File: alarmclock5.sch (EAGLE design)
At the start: 44 parts, among them Q1 FDN360P, T1 2N2222, X1 MKDSN1,5/2-5,08, X2 MKDSN1,5/2-5,08, X3 MKDSN1,5/2-5,08, X4 MKDSN1,5/2-5,08

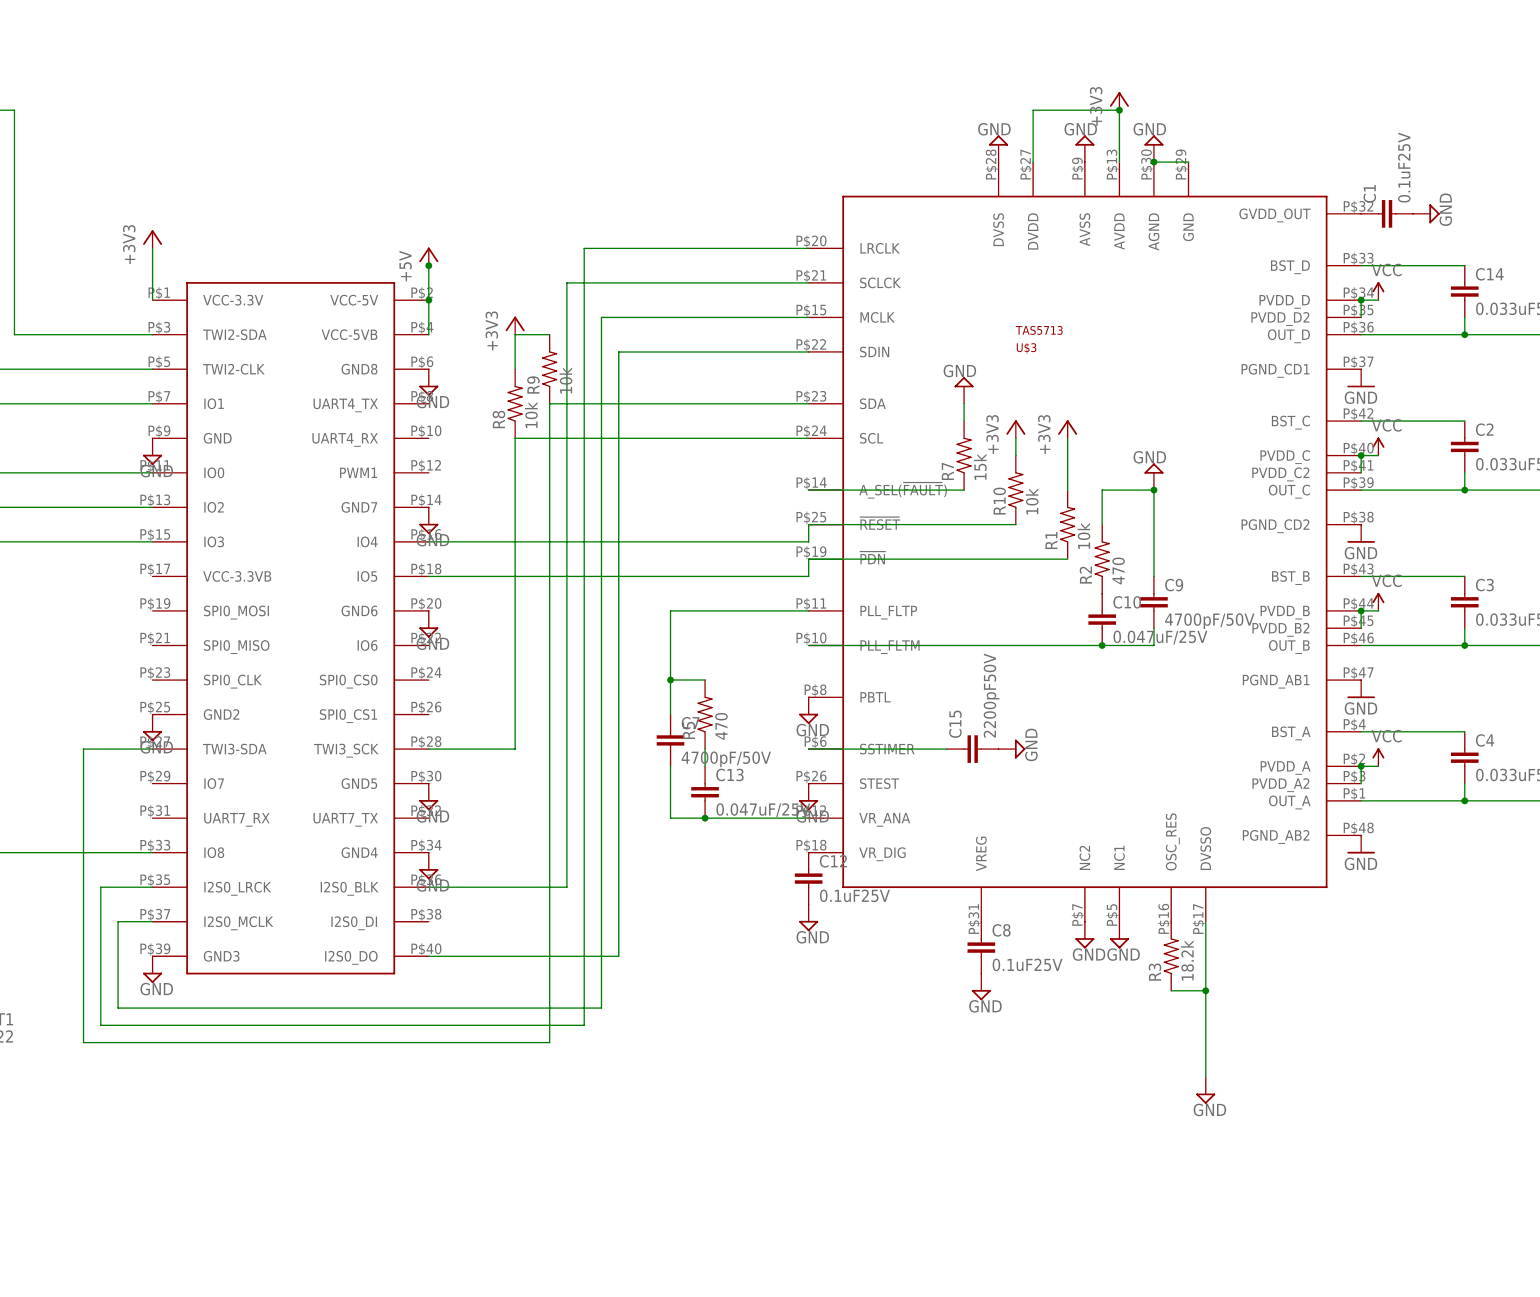
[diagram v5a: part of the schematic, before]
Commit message: new decoupling capa
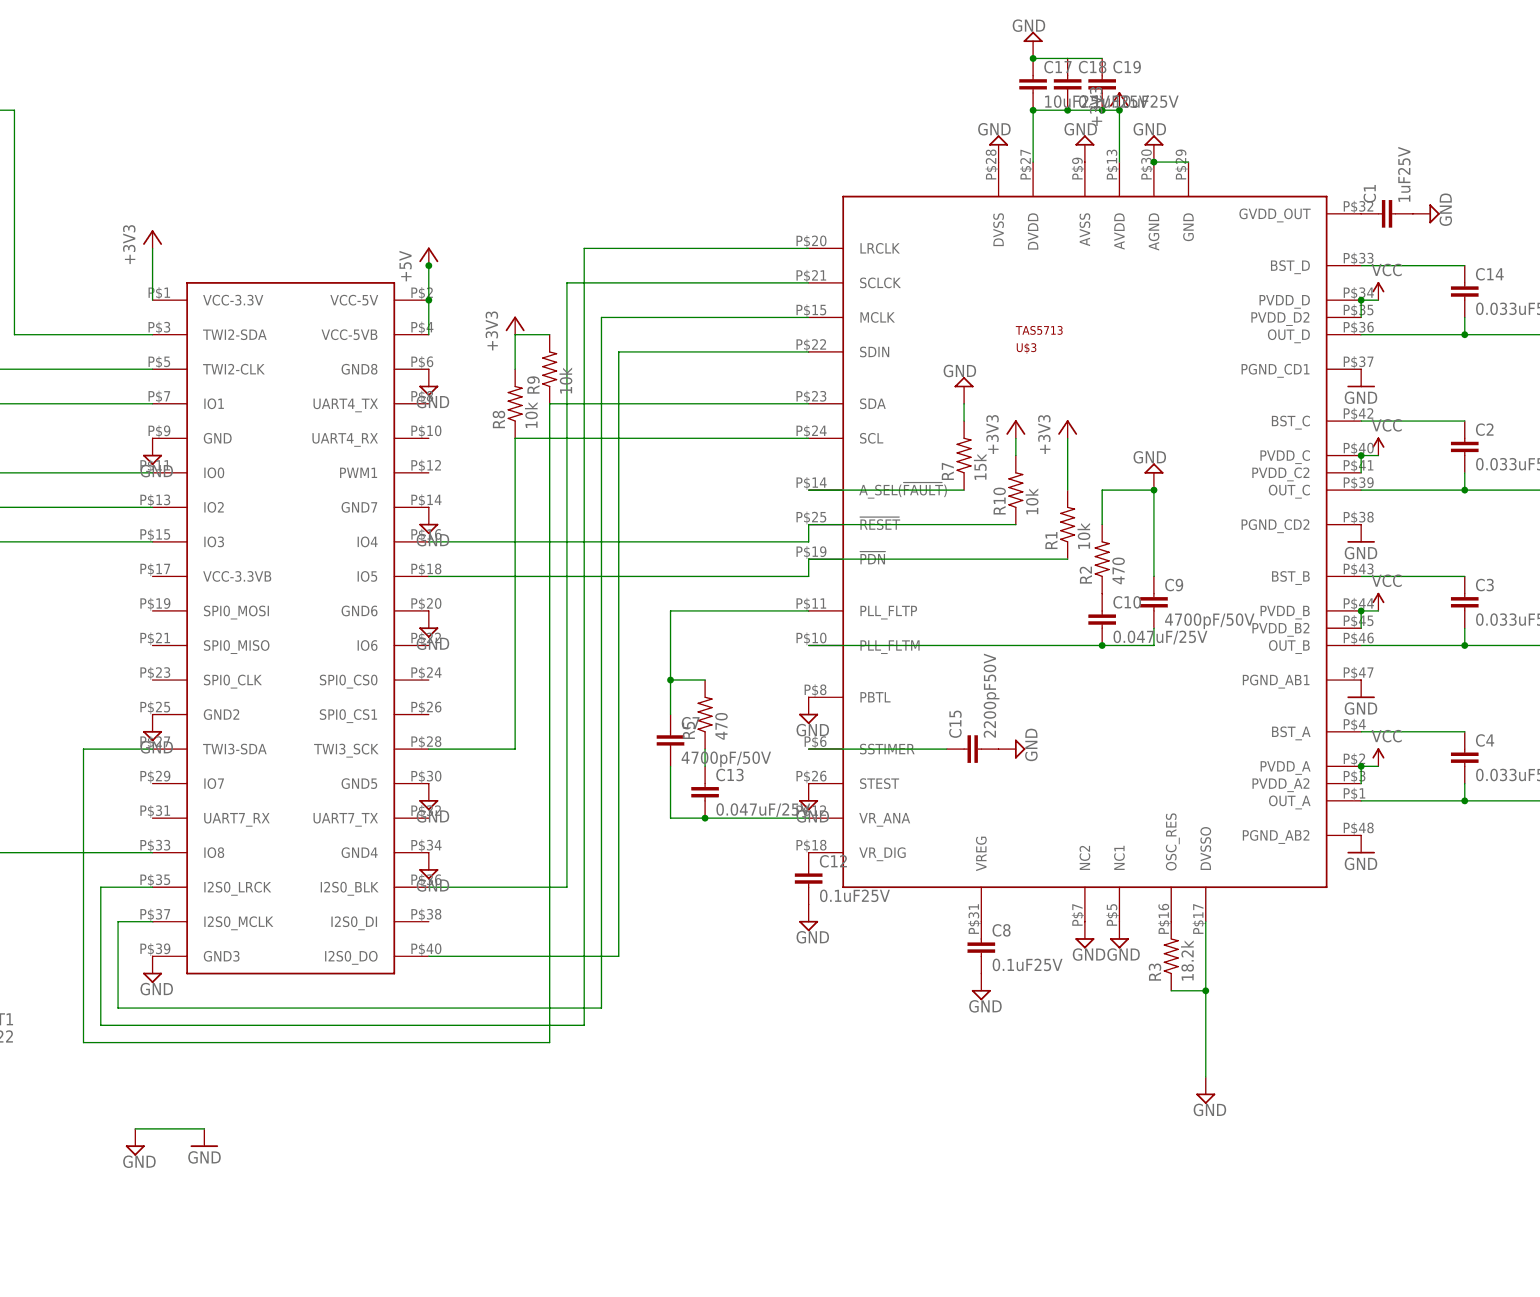
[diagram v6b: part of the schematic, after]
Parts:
- added C17, C19: 10uF25V, SparkFun-Capacitors:CAP0603-CAP
- added C18: 0.1uF25V, SparkFun-Capacitors:CAP0603-CAP
- C1: value 0.1uF25V -> 1uF25V
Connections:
- net +3V3: now also C17.2, C18.2, C19.2
- net GND: now also C17.1, C18.1, C19.1
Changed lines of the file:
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@@
 <part name="+3V8" library="supply1" deviceset="+3V3" device=""/>
 <part name="R10" library="SparkFun-Passives" deviceset="RESISTOR" device="0603-RES" value="10k"/>
-<part name="C1" library="SparkFun-Capacitors" deviceset="CAP" device="0603-CAP" value="0.1uF25V"/>
+<part name="C1" library="SparkFun-Capacitors" deviceset="CAP" device="0603-CAP" value="1uF25V"/>
 <part name="SUPPLY18" library="supply2" deviceset="GND" device=""/>
 <part name="C15" library="SparkFun-Capacitors" deviceset="CAP" device="0603-CAP" value="2200pF50V"/>
@@
 <part name="C16" library="SparkFun-Passives" deviceset="CAP_POL" device="PTH2" value="680uF/25V"/>
 <part name="R12" library="SparkFun-Passives" deviceset="RESISTOR" device="0603-RES" value="10k"/>
+<part name="SUPPLY1" library="supply2" deviceset="GND" device=""/>
+<part name="GND6" library="SparkFun-Aesthetics" deviceset="GND" device=""/>
+<part name="C17" library="SparkFun-Capacitors" deviceset="CAP" device="0603-CAP" value="10uF25V"/>
+<part name="SUPPLY32" library="supply2" deviceset="GND" device=""/>
+<part name="C18" library="SparkFun-Capacitors" deviceset="CAP" device="0603-CAP" value="0.1uF25V"/>
+<part name="C19" library="SparkFun-Capacitors" deviceset="CAP" device="0603-CAP" value="10uF25V"/>
 </parts>
 <sheets>
@@
 <instance part="C16" gate="G$1" x="-78.74" y="-101.6" rot="MR0"/>
 <instance part="R12" gate="G$1" x="-86.36" y="-104.14" rot="MR90"/>
+<instance part="SUPPLY1" gate="GND" x="-22.86" y="-106.68"/>
+<instance part="GND6" gate="1" x="-12.7" y="-106.68" rot="MR0"/>
+<instance part="C17" gate="G$1" x="109.22" y="48.26"/>
+<instance part="SUPPLY32" gate="GND" x="109.22" y="55.88" rot="R180"/>
+<instance part="C18" gate="G$1" x="114.3" y="48.26"/>
+<instance part="C19" gate="G$1" x="119.38" y="48.26"/>
 </instances>
 <busses>
@@
 <junction x="-78.74" y="-109.22"/>
 </segment>
+<segment>
+<pinref part="SUPPLY1" gate="GND" pin="GND"/>
+<pinref part="GND6" gate="1" pin="GND"/>
+<wire x1="-22.86" y1="-104.14" x2="-12.7" y2="-104.14" width="0.1524" layer="91"/>
+</segment>
+<segment>
+<pinref part="C17" gate="G$1" pin="1"/>
+<pinref part="SUPPLY32" gate="GND" pin="GND"/>
+<pinref part="C18" gate="G$1" pin="1"/>
+<wire x1="114.3" y1="53.34" x2="109.22" y2="53.34" width="0.1524" layer="91"/>
+<junction x="109.22" y="53.34"/>
+<pinref part="C19" gate="G$1" pin="1"/>
+<wire x1="114.3" y1="53.34" x2="119.38" y2="53.34" width="0.1524" layer="91"/>
+</segment>
 </net>
 <net name="N$1" class="0">
@@
 <pinref part="U$3" gate="G$1" pin="AVDD"/>
 <wire x1="121.92" y1="38.1" x2="121.92" y2="45.72" width="0.1524" layer="91"/>
-<wire x1="121.92" y1="45.72" x2="109.22" y2="45.72" width="0.1524" layer="91"/>
+<wire x1="121.92" y1="45.72" x2="119.38" y2="45.72" width="0.1524" layer="91"/>
 <pinref part="U$3" gate="G$1" pin="DVDD"/>
+<wire x1="119.38" y1="45.72" x2="114.3" y2="45.72" width="0.1524" layer="91"/>
+<wire x1="114.3" y1="45.72" x2="109.22" y2="45.72" width="0.1524" layer="91"/>
 <wire x1="109.22" y1="38.1" x2="109.22" y2="45.72" width="0.1524" layer="91"/>
 <pinref part="+3V3" gate="G$1" pin="+3V3"/>
 <junction x="121.92" y="45.72"/>
-</segment>
-<segment>
+<pinref part="C17" gate="G$1" pin="2"/>
+<junction x="109.22" y="45.72"/>
+<pinref part="C18" gate="G$1" pin="2"/>
+<junction x="114.3" y="45.72"/>
+<pinref part="C19" gate="G$1" pin="2"/>
+<junction x="119.38" y="45.72"/>
+</segment>
+<segment>
